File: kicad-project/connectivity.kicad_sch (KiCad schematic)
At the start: 5 parts

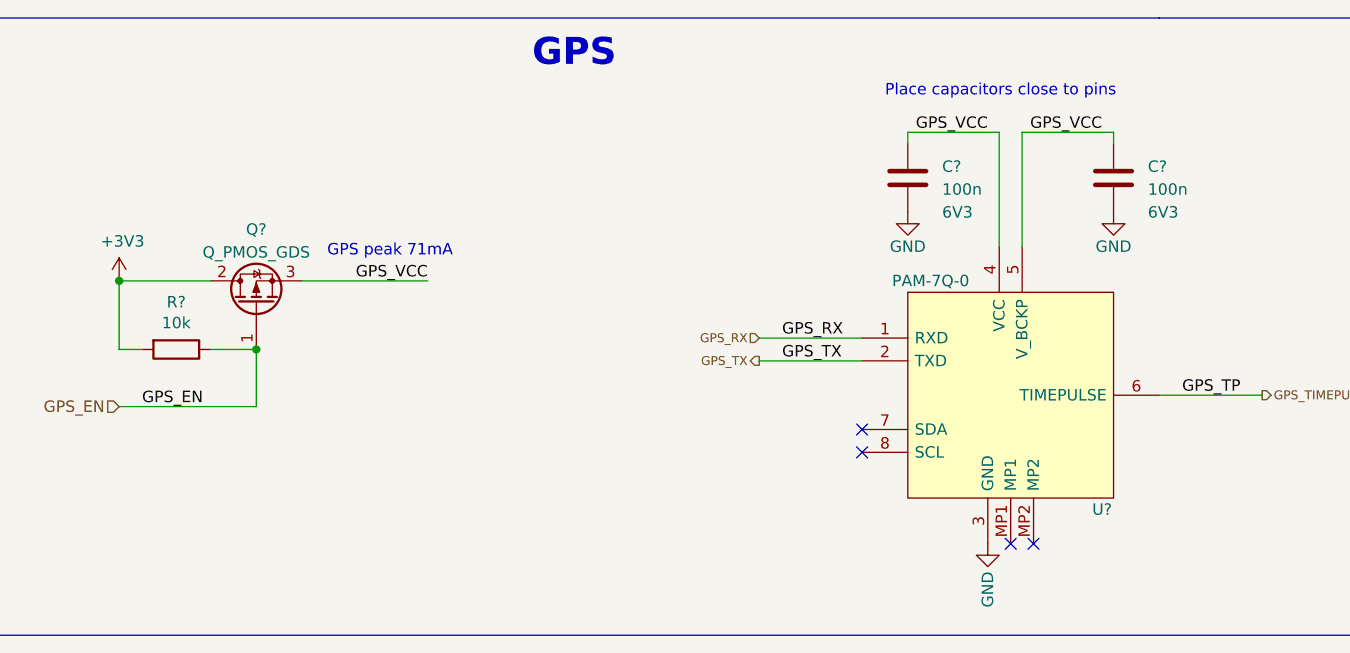
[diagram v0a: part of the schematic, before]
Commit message: hw: add footprints for resistors and capacitors and re-add specs documant that was deleted
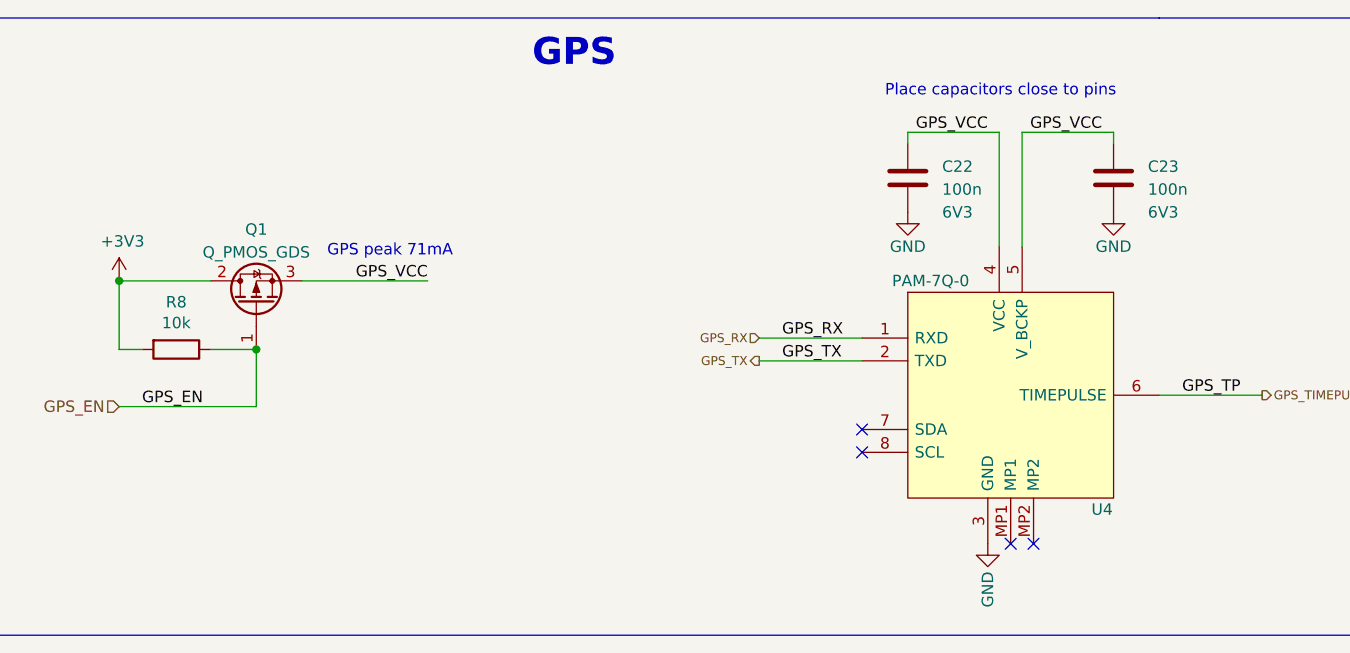
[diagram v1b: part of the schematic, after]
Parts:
- C22, C23: renamed from C?; footprint (none) -> Capacitor_SMD:C_0603_1608Metric
- R8: renamed from R?; footprint (none) -> Resistor_SMD:R_0603_1608Metric
- U4: renamed from U?; footprint PAM7Q0 -> (none)
- gave numbers to parts that had none: 1
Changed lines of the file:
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@@
   (symbol (lib_id "Device:R") (at 55.88 66.04 270) (unit 1)
     (in_bom yes) (on_board yes)
-    (property "Reference" "R?" (id 0) (at 55.88 60.7822 90))
+    (property "Reference" "R8" (id 0) (at 55.88 60.7822 90))
     (property "Value" "10k" (id 1) (at 55.88 63.0936 90))
-    (property "Footprint" "" (id 2) (at 55.88 64.262 90)
+    (property "Footprint" "Resistor_SMD:R_0603_1608Metric" (id 2) (at 55.88 64.262 90)
       (effects (font (size 1.27 1.27)) hide)
     )
@@
   (symbol (lib_id "power:+3V3") (at 49.53 58.42 0) (unit 1)
     (in_bom yes) (on_board yes)
-    (property "Reference" "#PWR0164" (id 0) (at 49.53 62.23 0)
+    (property "Reference" "#PWR047" (id 0) (at 49.53 62.23 0)
       (effects (font (size 1.27 1.27)) hide)
     )
@@
   (symbol (lib_id "power:GND") (at 146.05 87.63 0) (unit 1)
     (in_bom yes) (on_board yes)
-    (property "Reference" "#PWR0159" (id 0) (at 146.05 93.98 0)
+    (property "Reference" "#PWR049" (id 0) (at 146.05 93.98 0)
       (effects (font (size 1.27 1.27)) hide)
     )
@@
   (symbol (lib_id "Device:C") (at 160.02 46.99 0) (unit 1)
     (in_bom yes) (on_board yes)
-    (property "Reference" "C?" (id 0) (at 163.83 45.7199 0)
+    (property "Reference" "C23" (id 0) (at 163.83 45.7199 0)
       (effects (font (size 1.27 1.27)) (justify left))
     )
@@
       (effects (font (size 1.27 1.27)) (justify left))
     )
-    (property "Footprint" "" (id 2) (at 160.9852 50.8 0)
+    (property "Footprint" "Capacitor_SMD:C_0603_1608Metric" (id 2) (at 160.9852 50.8 0)
       (effects (font (size 1.27 1.27)) hide)
     )
@@
   (symbol (lib_id "power:GND") (at 137.16 50.8 0) (unit 1)
     (in_bom yes) (on_board yes)
-    (property "Reference" "#PWR0161" (id 0) (at 137.16 57.15 0)
+    (property "Reference" "#PWR048" (id 0) (at 137.16 57.15 0)
       (effects (font (size 1.27 1.27)) hide)
     )
@@
   (symbol (lib_id "Device:C") (at 137.16 46.99 0) (unit 1)
     (in_bom yes) (on_board yes)
-    (property "Reference" "C?" (id 0) (at 140.97 45.7199 0)
+    (property "Reference" "C22" (id 0) (at 140.97 45.7199 0)
       (effects (font (size 1.27 1.27)) (justify left))
     )
@@
       (effects (font (size 1.27 1.27)) (justify left))
     )
-    (property "Footprint" "" (id 2) (at 138.1252 50.8 0)
+    (property "Footprint" "Capacitor_SMD:C_0603_1608Metric" (id 2) (at 138.1252 50.8 0)
       (effects (font (size 1.27 1.27)) hide)
     )
@@
   (symbol (lib_id "power:GND") (at 160.02 50.8 0) (unit 1)
     (in_bom yes) (on_board yes)
-    (property "Reference" "#PWR0162" (id 0) (at 160.02 57.15 0)
+    (property "Reference" "#PWR050" (id 0) (at 160.02 57.15 0)
       (effects (font (size 1.27 1.27)) hide)
     )
@@
   (symbol (lib_id "PPSE_2021:PAM-7Q-0") (at 132.08 62.23 0) (unit 1)
     (in_bom yes) (on_board yes) (fields_autoplaced)
-    (property "Reference" "U?" (id 0) (at 158.75 83.82 0))
+    (property "Reference" "U4" (id 0) (at 158.75 83.82 0))
     (property "Value" "PAM-7Q-0" (id 1) (at 139.7 58.42 0))
-    (property "Footprint" "PAM7Q0" (id 2) (at 173.99 66.04 0)
+    (property "Footprint" "" (id 2) (at 173.99 66.04 0)
       (effects (font (size 1.27 1.27)) (justify left) hide)
     )
@@
   (symbol (lib_id "Device:Q_PMOS_GDS") (at 64.77 60.96 90) (unit 1)
     (in_bom yes) (on_board yes)
-    (property "Reference" "Q?" (id 0) (at 64.77 52.705 90))
+    (property "Reference" "Q1" (id 0) (at 64.77 52.705 90))
     (property "Value" "Q_PMOS_GDS" (id 1) (at 64.77 55.245 90))
     (property "Footprint" "" (id 2) (at 62.23 55.88 0)

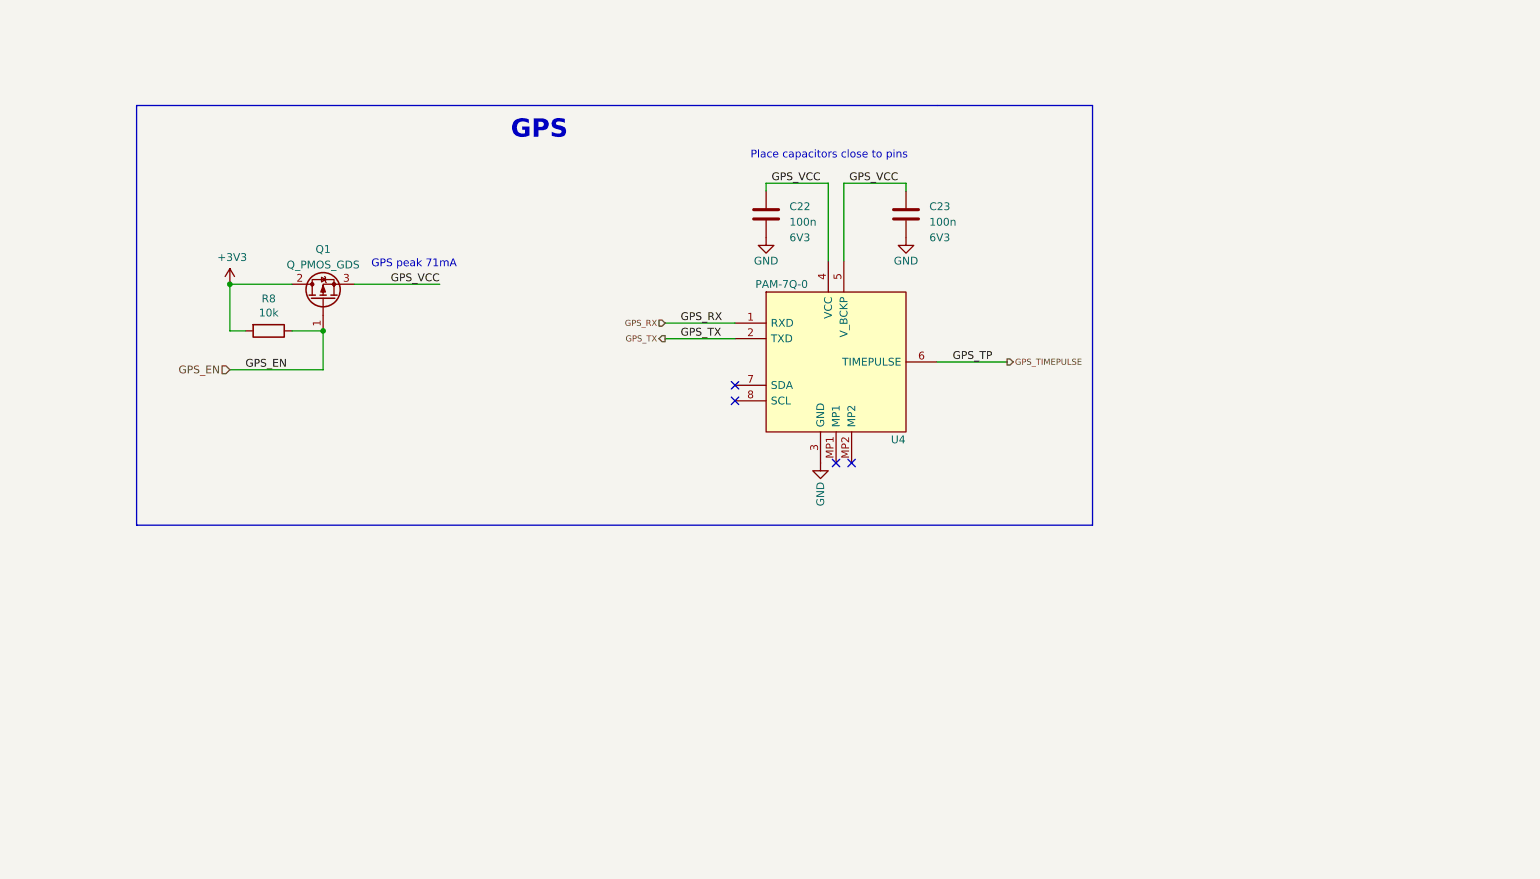
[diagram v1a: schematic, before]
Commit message: hw: part of last checks and footprint assignments
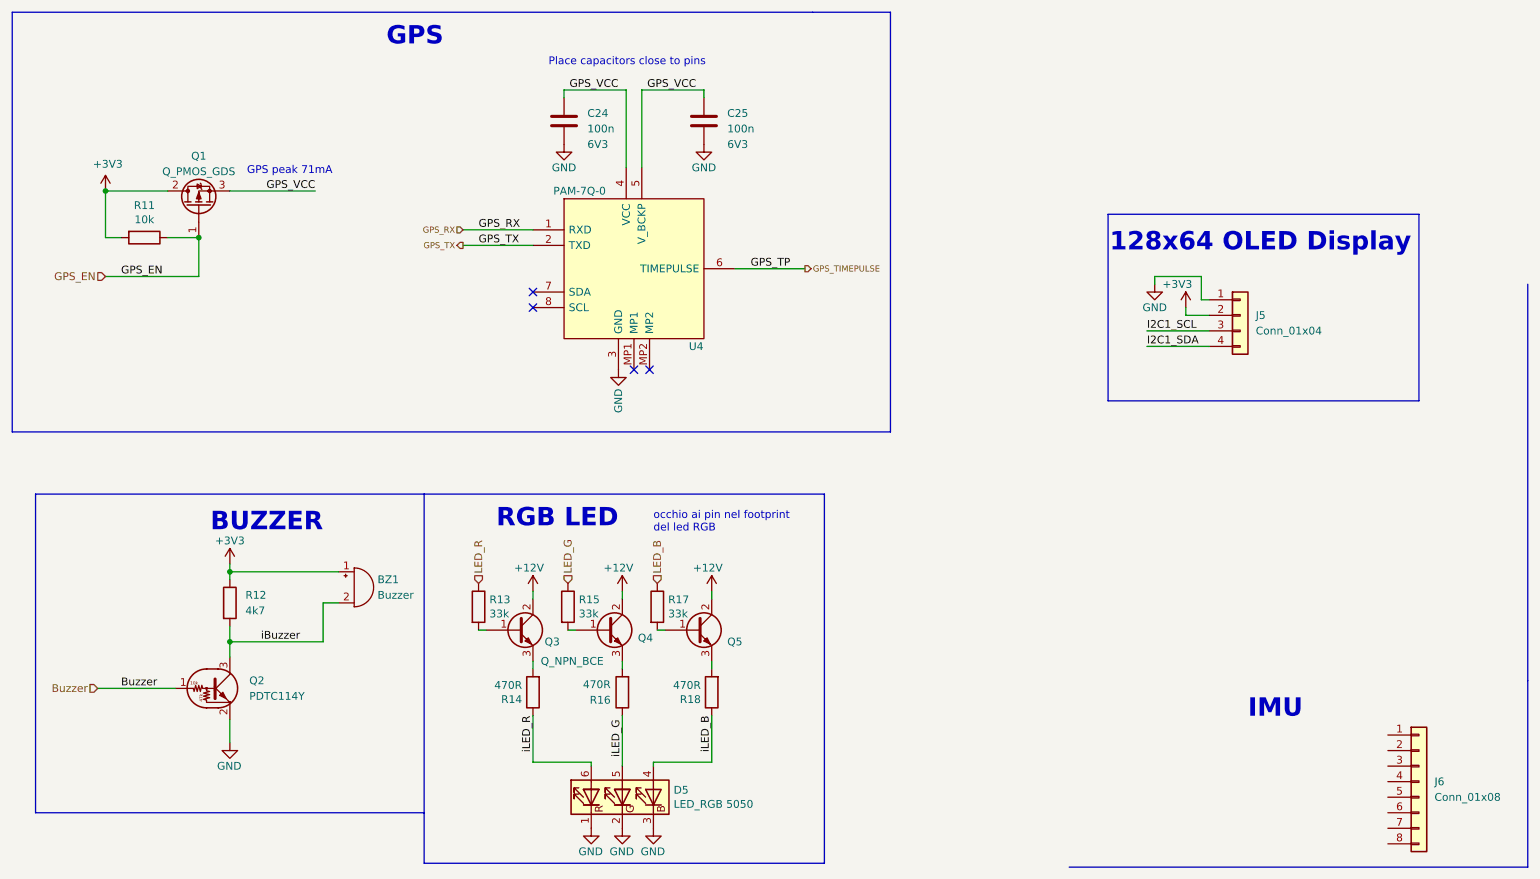
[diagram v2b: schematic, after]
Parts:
- added BZ1: Buzzer, Buzzer_Beeper:Buzzer_12x9.5RM7.6, symbol Device:Buzzer
- added D5: LED_RGB 5050, LED_SMD:LED_RGB_1210, symbol Device:LED_RGB
- added J5: Conn_01x04, Connector_PinHeader_2.54mm:PinHeader_1x04_P2.54mm_Vertical_SMD_Pin1Left, symbol Connector_Generic:Conn_01x04
- added J6: Conn_01x08, symbol Connector_Generic:Conn_01x08
- added Q2: PDTC114Y, symbol Transistor_BJT:DTC114Y
- added Q3: Q_NPN_BCE, symbol Device:Q_NPN_BCE
- added Q4, Q5: ~, symbol Device:Q_NPN_BCE
- added R12: 4k7, Resistor_SMD:R_0603_1608Metric, symbol Device:R
- added R13, R15, R17: 33k, Resistor_SMD:R_0603_1608Metric, symbol Device:R
- added R14, R16, R18: 470R, Resistor_SMD:R_0603_1608Metric, symbol Device:R
- renumbered C22 to C24, C23 to C25, R8 to R11
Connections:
- net +3V3: now also BZ1.1 (-), J5.2 (Pin_2), R12.1
- net GND: now also D5.1 (RK), D5.2 (GK), D5.3 (BK), J5.1 (Pin_1), Q2.2 (E)
- new net: Q3.3 (E), R14.2
- new net: Q4.1 (B), R15.2
- new net: Q3.1 (B), R13.2
- new net: Q4.3 (E), R16.2
- new net: Q5.1 (B), R17.2
- new net: Q5.3 (E), R18.2
- new net +12V: Q3.2 (C), Q4.2 (C), Q5.2 (C)
- new net Buzzer: Q2.1 (B)
- new net I2C1_SCL: J5.3 (Pin_3)
- new net I2C1_SDA: J5.4 (Pin_4)
- new net LED_B: R17.1
- new net LED_G: R15.1
- new net LED_R: R13.1
- new net iBuzzer: BZ1.2 (+), Q2.3 (C), R12.2
- new net iLED_B: D5.4 (BA), R18.1
- new net iLED_G: D5.5 (GA), R16.1
- new net iLED_R: D5.6 (RA), R14.1
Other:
- note added: "128x64 OLED Display"
- note added: "BUZZER"
- note added: "IMU"
- note added: "RGB LED"
- note added: "occhio ai pin nel footprint del led RGB"
- moved on the sheet: C24, C25, Q1, R11, U4

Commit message: hw: schematic updates
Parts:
- removed J6: Conn_01x08, symbol Connector_Generic:Conn_01x08
- added J?: Compass, symbol Connector_Generic:Conn_01x05
- added J?: Conn_01x08, symbol Connector_Generic:Conn_01x08
- Q1: value Q_PMOS_GDS -> 3LP01M; footprint (none) -> Package_TO_SOT_SMD:SOT-323_SC-70
- U4: footprint (none) -> ppse_2021:PAM-7Q0
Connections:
- net +3V3: now also J?.1 (Pin_1), J?.1 (Pin_1)
- net GND: now also J?.2 (Pin_2), J?.2 (Pin_2), J?.7 (Pin_7)
- new net DRDY: J?.5 (Pin_5)
- new net INT: J?.8 (Pin_8)
- new net SCL: J?.3 (Pin_3), J?.3 (Pin_3)
- new net SDA: J?.4 (Pin_4), J?.4 (Pin_4)
- no-connect marks 4 -> 6
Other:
- note added: "HMC5883L"
- note removed: "IMU"
